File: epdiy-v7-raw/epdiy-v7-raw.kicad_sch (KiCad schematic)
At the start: 109 parts, among them CN1 WP27D-S050VA3-R15000, IC1 MPU-6500, J1 USB_C_Receptacle_USB2.0, J2 EXTENSION_HEADER, J3 SIGNALS_HEADER, J4 XF2M-3315-1A, J5 CONN_BAT, J7 ESP_HDR, Q1 AO3401A, SW1 TC-0522C-1.7-160G, SW2 TC-0522C-1.7-160G, U1 RT9080-33GJ5, U10 ED060XC5, U11 TP4056, U3 TPS651851RSLR, U4 USBLC6-2P6, U8 ESP32-S3-WROOM-1, Y1 RV-3032-C7

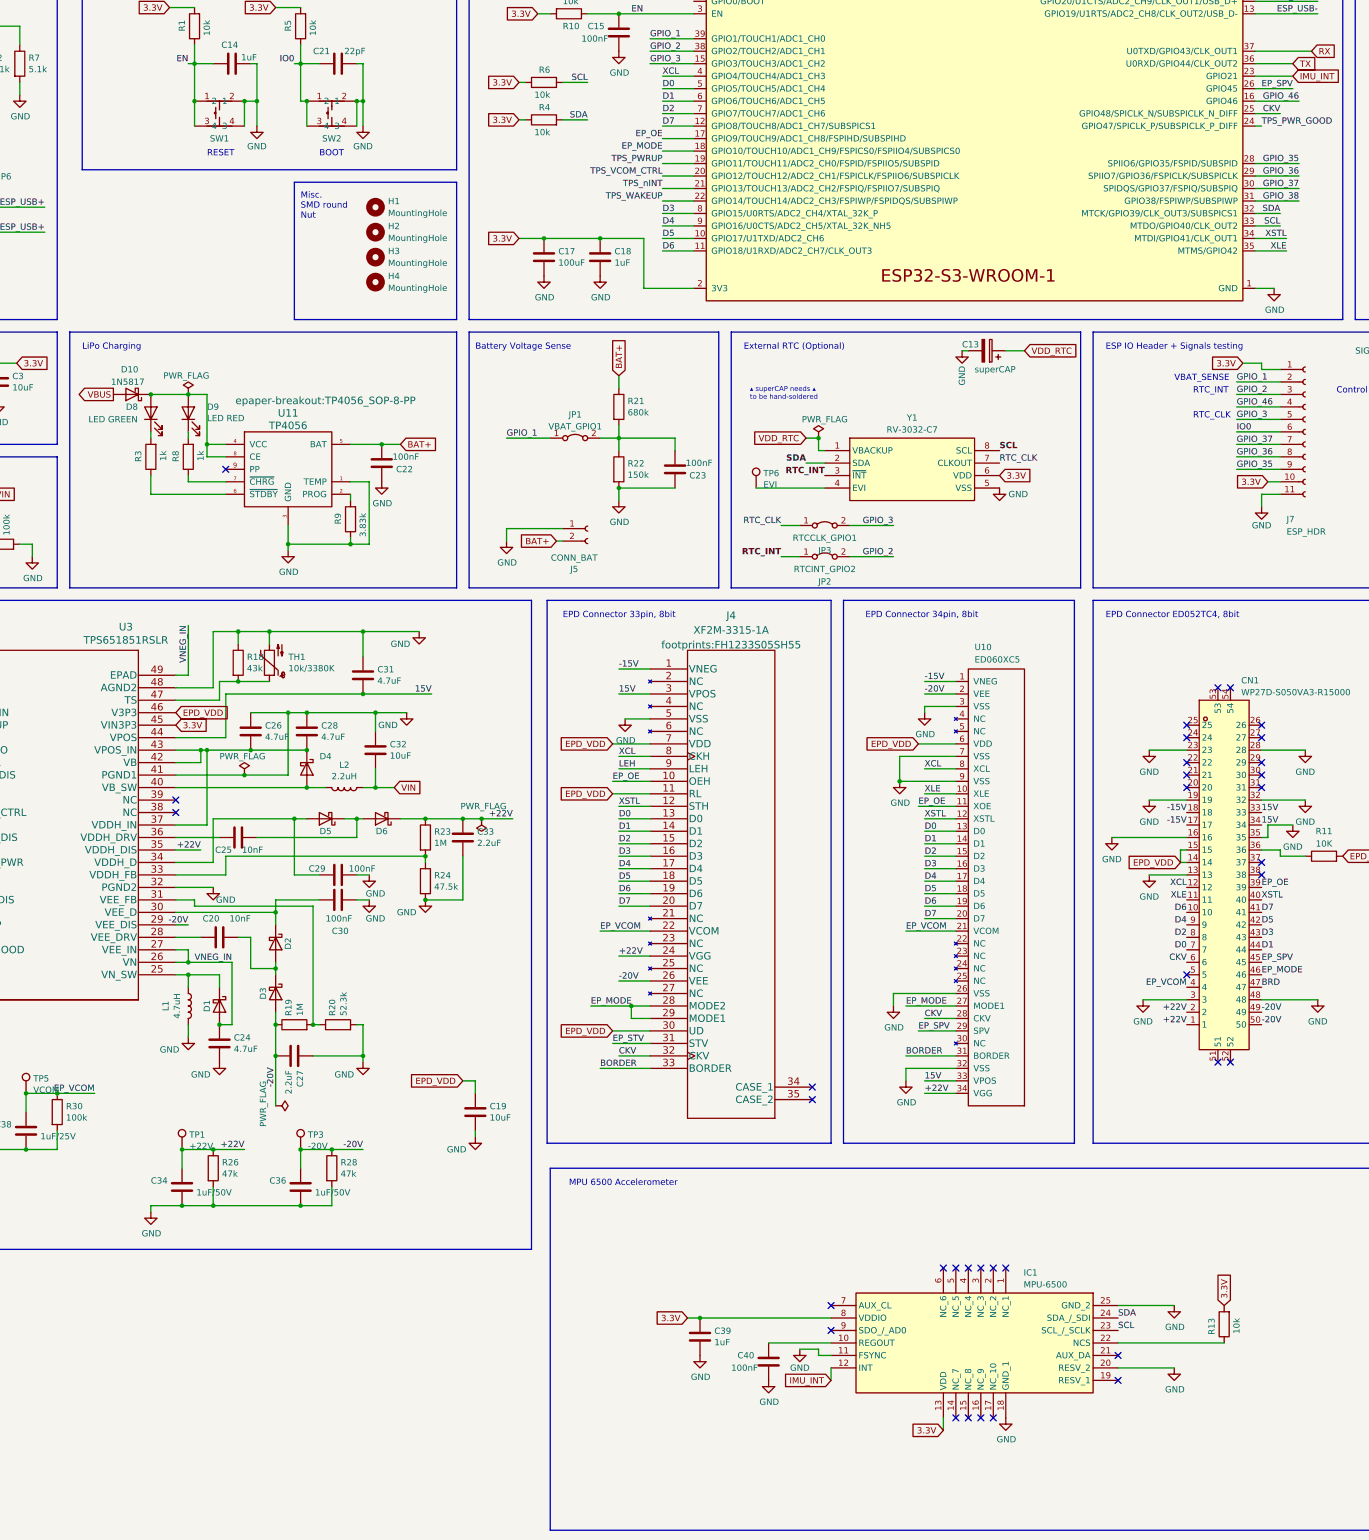
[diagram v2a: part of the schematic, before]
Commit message: Add MicroSD and fab files v1.0
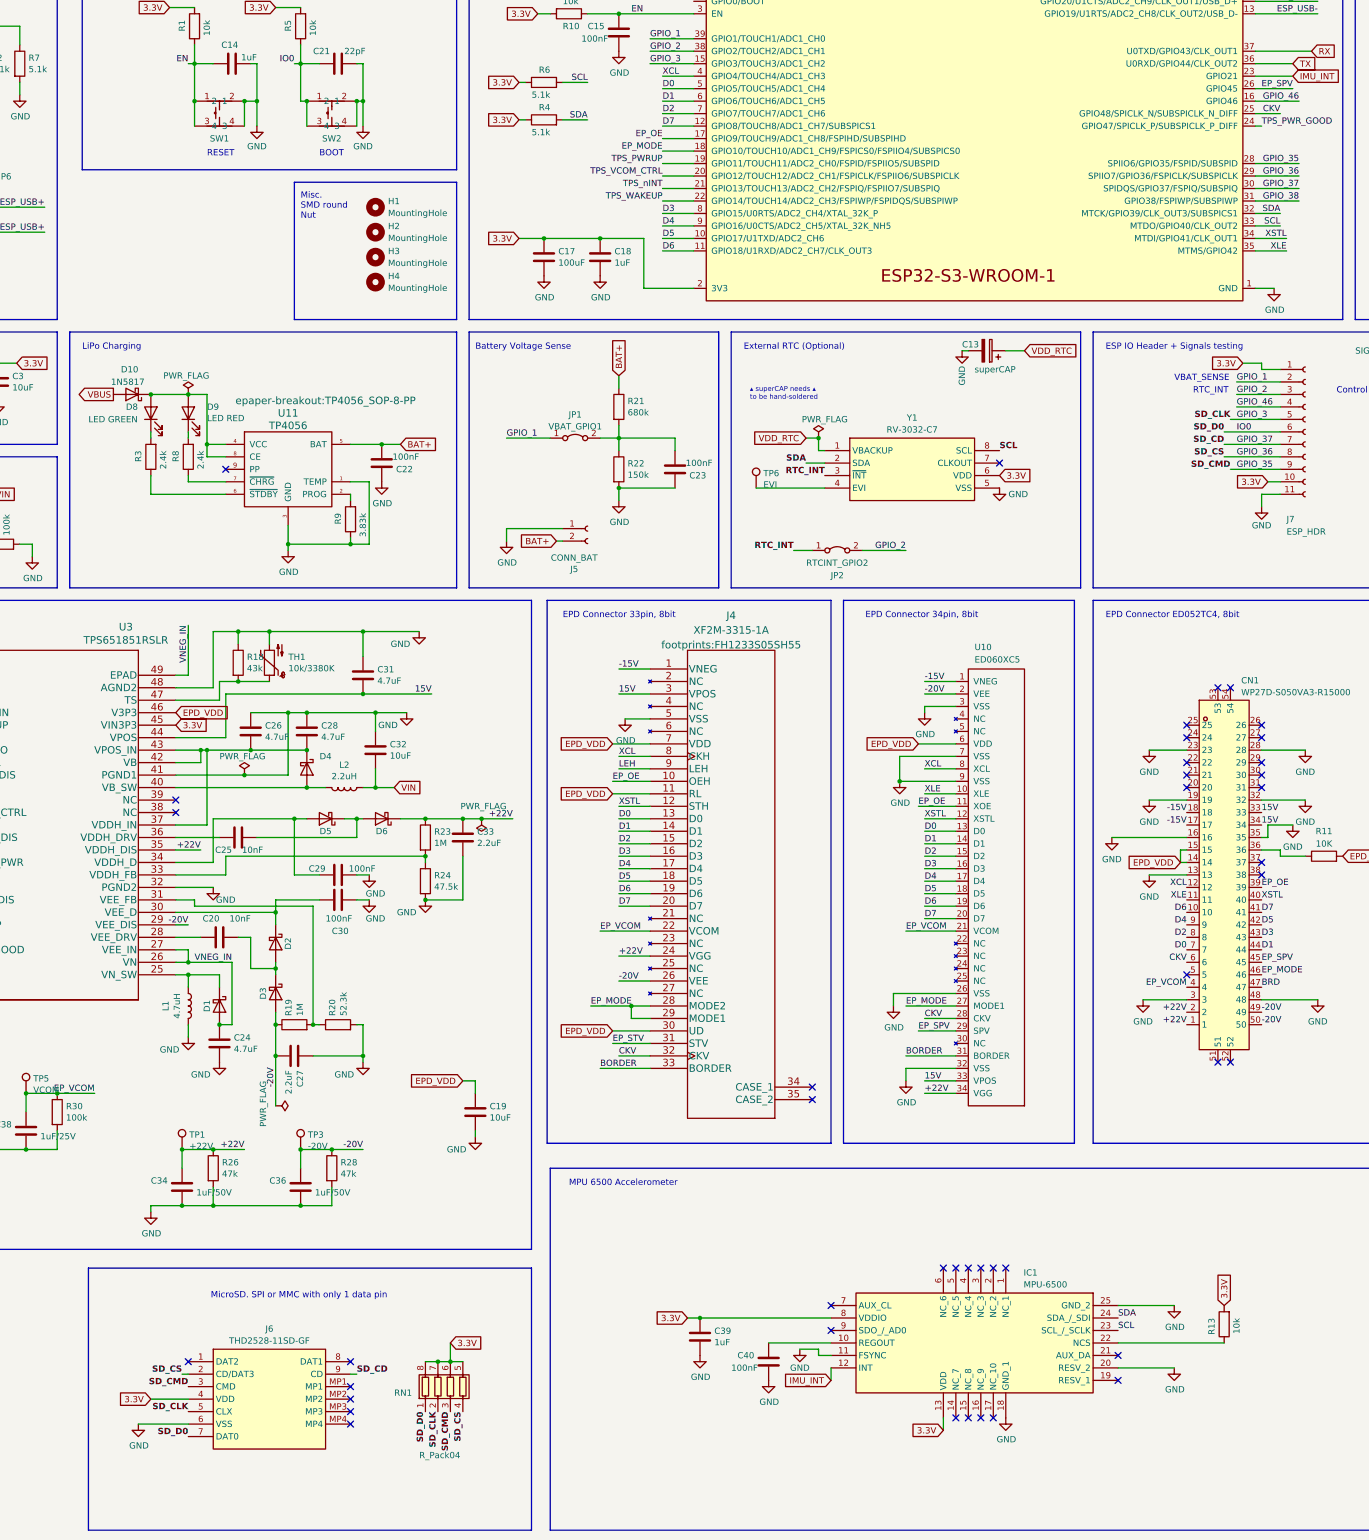
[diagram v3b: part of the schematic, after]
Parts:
- removed JP3: RTCCLK_GPIO1, Jumper:SolderJumper-2_P1.3mm_Bridged2Bar_Pad1.0x1.5mm, symbol Jumper:Jumper_2_Bridged
- added J6: THD2528-11SD-GF, footprints:MicroSD_THD252811SDGF, symbol MicroSD:THD2528-11SD-GF
- added RN1: R_Pack04, footprints:RESN_F392JTCE_UNR_SD-pullup, symbol Device:R_Pack04
- C17: LCSC C16133 -> C16133
- L1: LCSC C222947 -> C222947
- R3, R8: value 1k -> 2.4k; LCSC C21190 -> C22940
- R4, R6: value 10k -> 5.1k; LCSC C25804 -> C23186
- U11: LCSC C16581 -> C16581
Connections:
- net 3.3V: now also J6.4 (VDD), RN1.5 (R4.2), RN1.6 (R3.2), RN1.7 (R2.2), RN1.8 (R1.2)
- net GND: now also J6.6 (VSS)
- net GPIO_3: now also J6.5 (CLX), RN1.2 (R2.1)
- net GPIO_35: now also J6.3 (CMD), RN1.3 (R3.1)
- net GPIO_36: now also J6.2 (CD/DAT3), RN1.4 (R4.1)
- net GPIO_37: now also J6.9 (CD)
- net IO0: now also J6.7 (DAT0), RN1.1 (R1.1)
- net RTC_CLK: no longer names the net of Y1.7 (CLKOUT)
- no-connect marks 41 -> 48
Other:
- note added: "MicroSD. SPI or MMC with only 1 data pin"
- note removed: "RTC_CLK"
- moved on the sheet: JP2

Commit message: Update v7 raw
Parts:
- added R12, R14, R15: 10K, Resistor_SMD:R_0603_1608Metric, symbol Device:R
- added SW3, SW4, SW5: K2-1806SQ-A2DW-04, footprints:C5143621_KEY-SMD_TS24ZJ, symbol Side-button:K2-1806SQ-A2DW-04
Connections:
- net EN: now also SW1.4; no longer SW1.1
- net GND: now also SW1.1, SW2.1, R12.2, R14.2, R15.2; no longer SW1.4, SW2.4
- net GPIO_3: now also SW3.2
- net GPIO_38: now also SW5.2
- net GPIO_46: now also SW4.2
- net IO0: now also SW2.4; no longer SW2.1
- new net: R12.1, SW3.1
- new net: R15.1, SW5.1
- new net: R14.1, SW4.1
- no-connect marks 48 -> 57
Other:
- note added: "Side-push Buttons, 3, 46, 38"
- moved on the sheet: J3

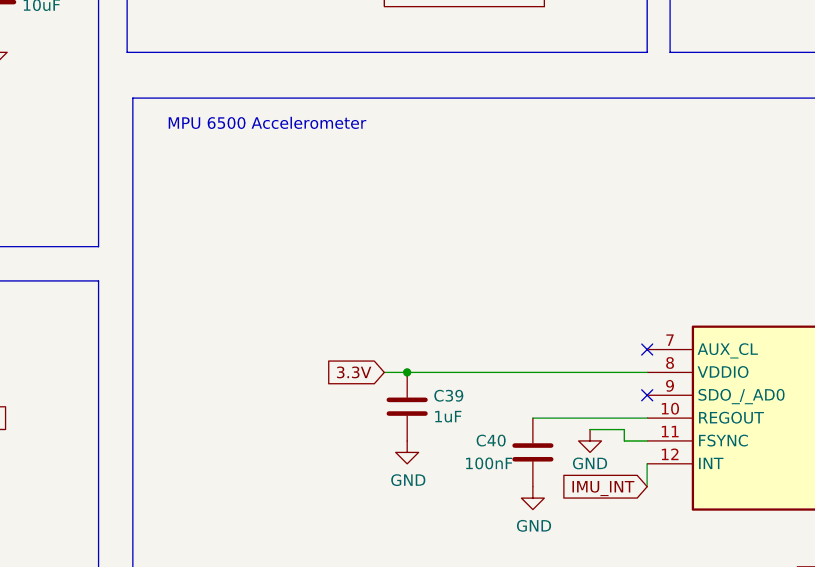
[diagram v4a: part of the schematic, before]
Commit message: 1.1 corrected IMU to 0x69
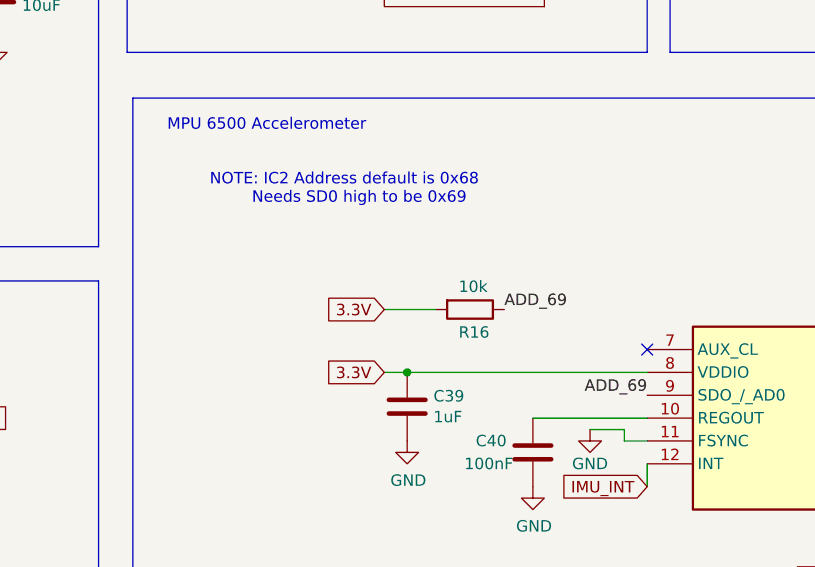
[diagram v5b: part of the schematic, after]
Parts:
- added R16: 10k, Resistor_SMD:R_0603_1608Metric, symbol Device:R
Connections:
- net 3.3V: now also R16.2
- net ADD_69: now reaches IC1.9 (SDO_/_AD0)
- net ADD_69: now also R16.1
- no-connect marks 57 -> 56
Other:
- note added: "NOTE: IC2 Address default is 0x68 Needs SD0 high to be 0x69"
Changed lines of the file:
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@@
 	)
 	(no_connect
-		(at 281.94 313.69)
-	)
-	(no_connect
 		(at 369.57 190.5)
 	)
@@
 		)
 	)
+	(wire
+		(pts
+			(xy 252.73 304.165) (xy 258.445 304.165)
+		)
+		(stroke
+			(width 0)
+			(type default)
+		)
+	)
 	(polyline
 		(pts
@@
 		)
 	)
+	(text "NOTE: IC2 Address default is 0x68\n      Needs SD0 high to be 0x69"
+		(exclude_from_sim no)
+		(at 248.285 290.83 0)
+		(effects
+			(font
+				(size 1.27 1.27)
+			)
+		)
+	)
 	(text "Start pulse SOURCE"
 		(exclude_from_sim no)
@@
 		)
 	)
+	(label "ADD_69"
+		(at 266.065 304.165 0)
+		(effects
+			(font
+				(size 1.27 1.27)
+			)
+			(justify left bottom)
+		)
+	)
 	(label "XSTL"
 		(at 369.57 226.06 0)
@@
 		)
 	)
+	(label "ADD_69"
+		(at 281.94 313.69 180)
+		(effects
+			(font
+				(size 1.27 1.27)
+			)
+			(justify right bottom)
+		)
+	)
 	(label "D1"
 		(at 300.99 214.63 0)
@@
 	(global_label "3.3V"
 		(shape input)
+		(at 252.73 304.165 180)
+		(fields_autoplaced yes)
+		(effects
+			(font
+				(size 1.27 1.27)
+			)
+			(justify right)
+		)
+		(property "Intersheetrefs" "${INTERSHEET_REFS}"
+			(at 246.2866 304.165 0)
+			(effects
+				(font
+					(size 1.27 1.27)
+				)
+				(justify right)
+				(hide yes)
+			)
+		)
+		(property "Referenzen zwischen Schaltplänen" "${INTERSHEET_REFS}"
+			(at 252.73 306.0002 0)
+			(effects
+				(font
+					(size 1.27 1.27)
+				)
+				(justify right)
+				(hide yes)
+			)
+		)
+	)
+	(global_label "3.3V"
+		(shape input)
 		(at 361.95 308.61 90)
 		(fields_autoplaced yes)
@@
 					(unit 1)
 				)
+			)
+		)
+	)
+	(symbol
+		(lib_id "Device:R")
+		(at 262.255 304.165 270)
+		(unit 1)
+		(exclude_from_sim no)
+		(in_bom yes)
+		(on_board yes)
+		(dnp no)
+		(property "Reference" "R16"
+			(at 260.985 306.705 90)
+			(effects
+				(font
+					(size 1.27 1.27)
+				)
+				(justify left)
+			)
+		)
+		(property "Value" "10k"
+			(at 260.985 301.625 90)
+			(effects
+				(font
+					(size 1.27 1.27)
+				)
+				(justify left)
+			)
+		)
+		(property "Footprint" "Resistor_SMD:R_0603_1608Metric"
+			(at 262.255 302.387 90)
+			(effects
+				(font
+					(size 1.27 1.27)
+				)
+				(hide yes)
+			)
+		)
+		(property "Datasheet" "~"
+			(at 262.255 304.165 0)
+			(effects
+				(font
+					(size 1.27 1.27)
+				)
+				(hide yes)
+			)
+		)
+		(property "Description" ""
+			(at 262.255 304.165 0)
+			(effects
+				(font
+					(size 1.27 1.27)
+				)
+				(hide yes)
+			)
+		)
+		(property "LCSC" "C25804"
+			(at 262.255 304.165 90)
+			(effects
+				(font
+					(size 1.27 1.27)
+				)
+				(hide yes)
+			)
+		)
+		(pin "1"
+		)
+		(pin "2"
+		)
+		(instances
+			(project "epdiy-v7-raw"
+				(path "/d463a158-2b18-43e0-b0c5-d5462331aab1"
+					(reference "R16")
+					(unit 1)
+				)

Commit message: 1.1 is ready
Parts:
- removed C16: 10uF, Capacitor_SMD:C_0805_2012Metric, symbol Device:C
- removed C21: 22pF, Capacitor_SMD:C_0402_1005Metric, symbol Device:C
- removed C22: 100nF, Capacitor_SMD:C_0805_2012Metric, symbol Device:C
- removed J5: CONN_BAT, Connector_PinHeader_2.54mm:PinHeader_1x02_P2.54mm_Vertical, symbol Connector:Conn_01x02_Female
- removed J7: ESP_HDR, Connector_PinHeader_2.54mm:PinHeader_1x11_P2.54mm_Vertical, symbol Connector:Conn_01x11_Socket
- removed JP1: VBAT_GPIO1, Jumper:SolderJumper-2_P1.3mm_Bridged2Bar_Pad1.0x1.5mm, symbol Jumper:Jumper_2_Bridged
- removed SW2: TC-0522C-1.7-160G, footprints:C2845289_SW-SMD_4P-L5.2-W5.2-P3.70-LS6.4, symbol BUTTON:TC-0522C-1.7-160G
- added J5: S2B-PH-SM4-TB_LF__SN_, footprints:S2BPHSM4TBLFSN, symbol Battery:S2B-PH-SM4-TB_LF__SN_
- C15: value 100nF -> 22pF; footprint Capacitor_SMD:C_0805_2012Metric -> Capacitor_SMD:C_0402_1005Metric; LCSC C49678 -> C5119318
- JP2: footprint Jumper:SolderJumper-2_P1.3mm_Bridged2Bar_Pad1.0x1.5mm -> Jumper:SolderJumper-2_P1.3mm_Open_Pad1.0x1.5mm; symbol Jumper:Jumper_2_Bridged -> Jumper:Jumper_2_Open
- R12: value 10K -> 1k; footprint Resistor_SMD:R_0603_1608Metric -> Resistor_SMD:R_0402_1005Metric; LCSC C25804 -> C21190
- R3: value 2.4k -> 5.1k; LCSC C22940 -> C23186
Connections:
- net BAT+: now also J5.2
- net EN: no longer C15.1
- net GND: now also C15.1, J5.1; no longer C15.2
- net GPIO_1: now also C23.2, R21.2, R22.1
- net GPIO_2: now also J6.7 (DAT0), RN1.1 (R1.1)
- net GPIO_3: no longer SW3.2
- net GPIO_35: no longer J6.3 (CMD), RN1.3 (R3.1)
- net GPIO_36: no longer J6.2 (CD/DAT3), RN1.4 (R4.1)
- net GPIO_37: no longer J6.9 (CD)
- net IO0: now also C15.2, SW3.2; no longer J6.7 (DAT0), RN1.1 (R1.1)
- net SCL: now also J2.3 (Pin_3); no longer J2.4 (Pin_4)
- net SDA: now also J2.4 (Pin_4); no longer J2.3 (Pin_3)
- net RX renamed SD_CMD
- net SD_CMD: now also J6.3 (CMD), RN1.3 (R3.1)
- net TX renamed SD_CS
- net SD_CS: now also J6.2 (CD/DAT3), RN1.4 (R4.1)
- no-connect marks 56 -> 60
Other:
- note added: "Battery connector"
- note added: "OCTAL PSRAM DO NOT *USE*"
- note added: "RST Push switch"
- note added: "Side-push Buttons, 0, 46, 38"
- note added: "Signals testing"
- note added: "shared w/BOOT"
- note removed: "BOOT"
- note removed: "ESP IO Header + Signals testing"
- note removed: "RST & BOOT Push switches"
- note removed: "RTC_INT"
- note removed: "Side-push Buttons, 3, 46, 38"
- note removed: "VBAT_SENSE"
- moved on the sheet: C23, R10, R21, R22
